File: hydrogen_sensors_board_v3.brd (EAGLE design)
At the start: 100 x 100 mm, 97 parts, among them CN1 1X4-CLEANBIG, IC1 317T, IC2 LM741D, U1 ATMEGA328P_TQFP, Y1 16MHz

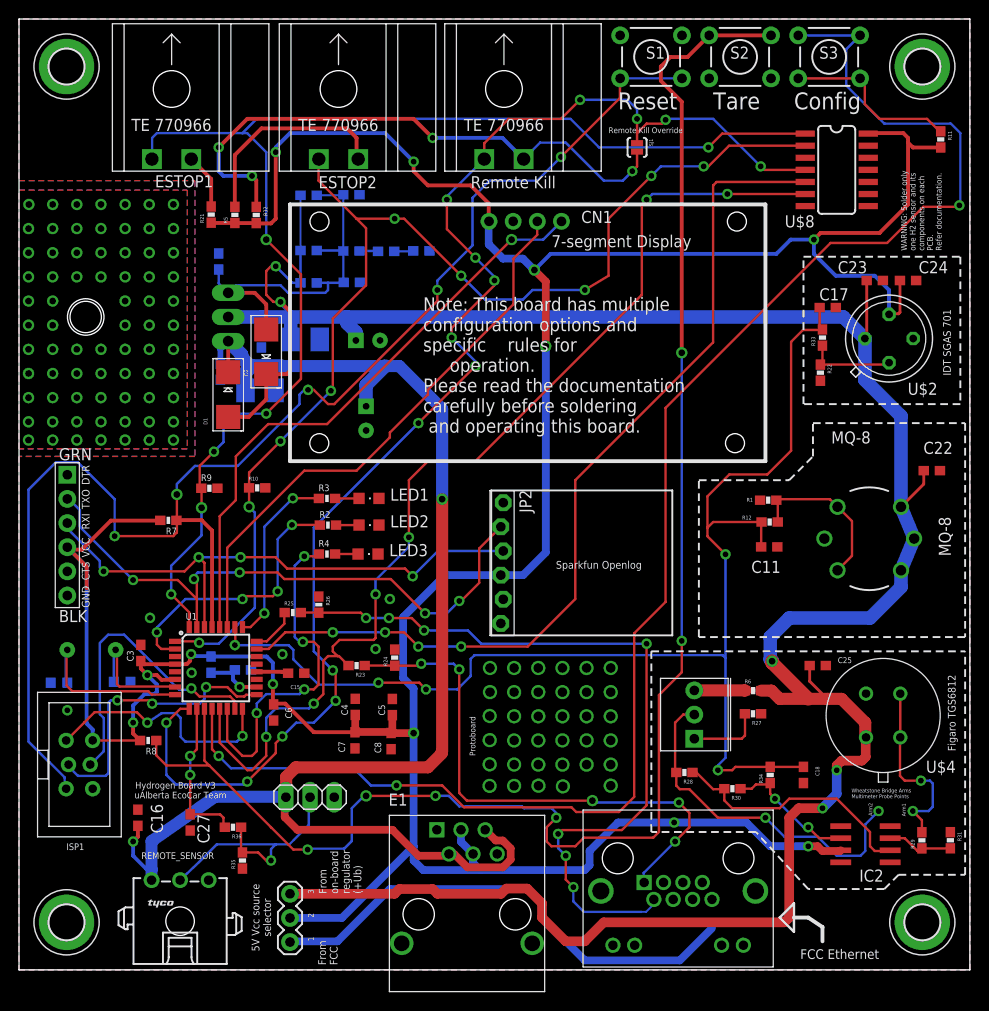
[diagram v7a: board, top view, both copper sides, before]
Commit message: routed ESTOP Signal
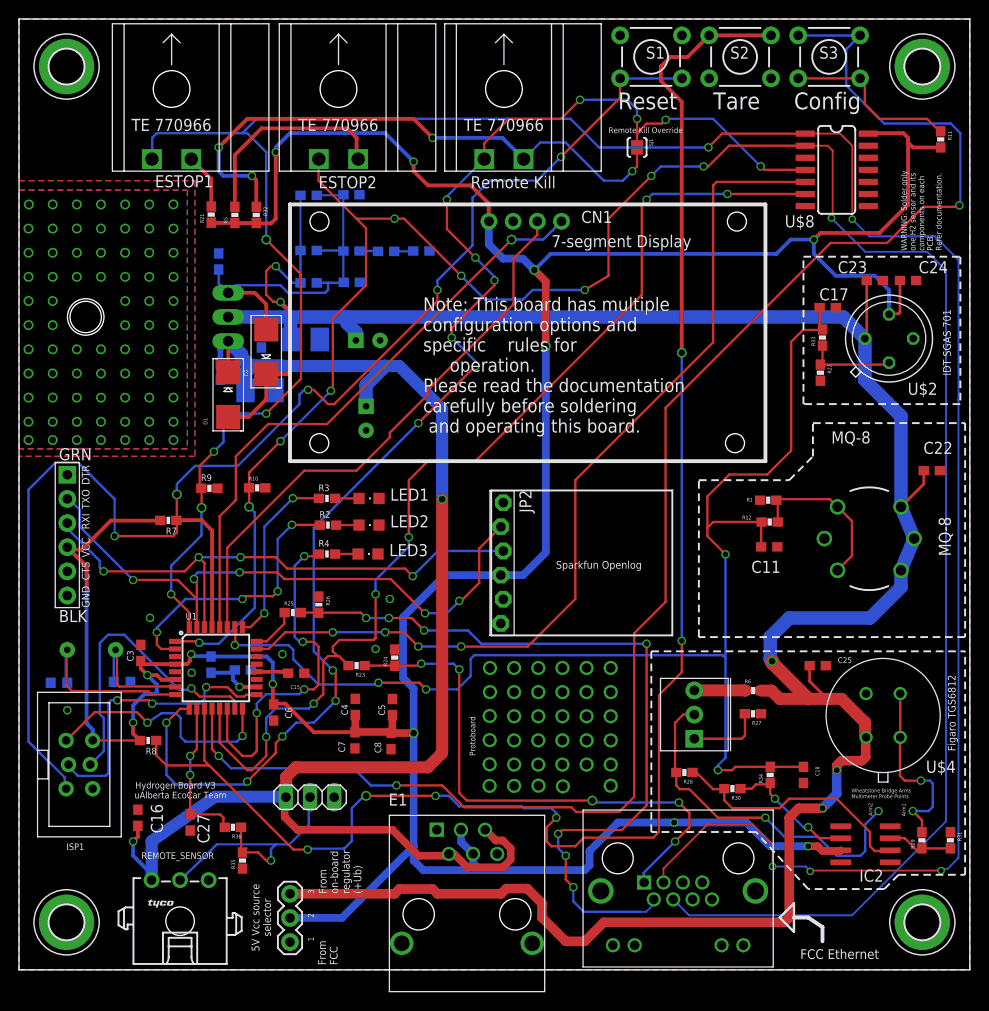
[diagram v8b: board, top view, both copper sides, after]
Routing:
- net ESTOP1: track 137.1 -> 264.9 mm, vias 6 -> 10
- net ESTOP2: track 125.4 -> 241.4 mm, vias 9 -> 10
- net 5V_FROM_FCC: track 52.9 -> 0.43 mm
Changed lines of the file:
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@@
 </class>
 </classes>
-<designrules name="SparkFun">
+<designrules name="SeeedStudio_2layer_DRU_no_angle_20140221">
+<description language="de">&lt;b&gt;EAGLE Design Rules&lt;/b&gt;
+&lt;p&gt;
+Die Standard-Design-Rules sind so gewählt, dass sie für
+die meisten Anwendungen passen. Sollte ihre Platine
+besondere Anforderungen haben, treffen Sie die erforderlichen
+Einstellungen hier und speichern die Design Rules unter
+einem neuen Namen ab.</description>
 <description language="en">&lt;b&gt;EAGLE Design Rules&lt;/b&gt;
 &lt;p&gt;
@@
 necessary adjustments and save your customized
 design rules under a new name.</description>
+<description language="zh">&lt;b&gt;Seeed Studio EAGLE Design Rules&lt;/b&gt;
+</description>
 <param name="layerSetup" value="(1*16)"/>
-<param name="mtCopper" value="0.035mm 0.035mm 0.035mm 0.035mm 0.035mm 0.035mm 0.035mm 0.035mm 0.035mm 0.035mm 0.035mm 0.035mm 0.035mm 0.035mm 0.035mm 0.035mm"/>
-<param name="mtIsolate" value="1.5mm 0.15mm 0.2mm 0.15mm 0.2mm 0.15mm 0.2mm 0.15mm 0.2mm 0.15mm 0.2mm 0.15mm 0.2mm 0.15mm 0.2mm"/>
-<param name="mdWireWire" value="8mil"/>
-<param name="mdWirePad" value="8mil"/>
-<param name="mdWireVia" value="8mil"/>
-<param name="mdPadPad" value="8mil"/>
-<param name="mdPadVia" value="8mil"/>
-<param name="mdViaVia" value="8mil"/>
-<param name="mdSmdPad" value="8mil"/>
-<param name="mdSmdVia" value="8mil"/>
-<param name="mdSmdSmd" value="8mil"/>
+<param name="mtCopper" value="0.035mm 0.0175mm 0.035mm 0.035mm 0.035mm 0.035mm 0.035mm 0.035mm 0.035mm 0.035mm 0.035mm 0.035mm 0.035mm 0.035mm 0.0175mm 0.035mm"/>
+<param name="mtIsolate" value="1.5mm 1.1mm 0.2mm 0.15mm 0.2mm 0.15mm 0.2mm 0.15mm 0.2mm 0.15mm 0.2mm 0.15mm 0.2mm 0.15mm 0.2mm"/>
+<param name="mdWireWire" value="6mil"/>
+<param name="mdWirePad" value="6mil"/>
+<param name="mdWireVia" value="6mil"/>
+<param name="mdPadPad" value="6mil"/>
+<param name="mdPadVia" value="6mil"/>
+<param name="mdViaVia" value="6mil"/>
+<param name="mdSmdPad" value="0mil"/>
+<param name="mdSmdVia" value="0mil"/>
+<param name="mdSmdSmd" value="0mil"/>
 <param name="mdViaViaSameLayer" value="8mil"/>
 <param name="mnLayersViaInSmd" value="2"/>
 <param name="mdCopperDimension" value="10mil"/>
-<param name="mdDrill" value="8mil"/>
+<param name="mdDrill" value="10mil"/>
 <param name="mdSmdStop" value="0mil"/>
-<param name="msWidth" value="8mil"/>
-<param name="msDrill" value="20mil"/>
-<param name="msMicroVia" value="9.99mm"/>
+<param name="msWidth" value="6mil"/>
+<param name="msDrill" value="12mil"/>
+<param name="msMicroVia" value="12mil"/>
 <param name="msBlindViaRatio" value="0.5"/>
 <param name="rvPadTop" value="0.25"/>
@@
 <param name="rvMicroViaOuter" value="0.25"/>
 <param name="rvMicroViaInner" value="0.25"/>
-<param name="rlMinPadTop" value="12mil"/>
+<param name="rlMinPadTop" value="10mil"/>
 <param name="rlMaxPadTop" value="20mil"/>
 <param name="rlMinPadInner" value="10mil"/>
 <param name="rlMaxPadInner" value="20mil"/>
-<param name="rlMinPadBottom" value="12mil"/>
+<param name="rlMinPadBottom" value="10mil"/>
 <param name="rlMaxPadBottom" value="20mil"/>
-<param name="rlMinViaOuter" value="10mil"/>
+<param name="rlMinViaOuter" value="6mil"/>
 <param name="rlMaxViaOuter" value="20mil"/>
-<param name="rlMinViaInner" value="10mil"/>
+<param name="rlMinViaInner" value="6mil"/>
 <param name="rlMaxViaInner" value="20mil"/>
 <param name="rlMinMicroViaOuter" value="4mil"/>
@@
 <param name="psTop" value="-1"/>
 <param name="psBottom" value="-1"/>
-<param name="psFirst" value="-1"/>
+<param name="psFirst" value="0"/>
 <param name="psElongationLong" value="100"/>
 <param name="psElongationOffset" value="100"/>
 <param name="mvStopFrame" value="1"/>
 <param name="mvCreamFrame" value="0"/>
-<param name="mlMinStopFrame" value="4mil"/>
-<param name="mlMaxStopFrame" value="4mil"/>
+<param name="mlMinStopFrame" value="2mil"/>
+<param name="mlMaxStopFrame" value="2mil"/>
 <param name="mlMinCreamFrame" value="0mil"/>
 <param name="mlMaxCreamFrame" value="0mil"/>
-<param name="mlViaStopLimit" value="25mil"/>
+<param name="mlViaStopLimit" value="100mil"/>
 <param name="srRoundness" value="0"/>
 <param name="srMinRoundness" value="0mil"/>
@@
 <param name="checkAngle" value="0"/>
 <param name="checkFont" value="1"/>
-<param name="checkRestrict" value="1"/>
+<param name="checkRestrict" value="0"/>
 <param name="checkStop" value="0"/>
 <param name="checkValues" value="0"/>
@@
 <wire x1="19" y1="50.82" x2="19.17" y2="50.65" width="0.254" layer="1"/>
 <contactref element="ETH1" pad="P$3"/>
-<wire x1="17.901" y1="36.0426" x2="67.78" y2="9.19" width="0" layer="19" extent="1-1"/>
+<wire x1="82.6853" y1="87.945" x2="86.3498" y2="87.945" width="0.2032" layer="1"/>
+<wire x1="86.3498" y1="87.945" x2="87.63" y2="86.6648" width="0.2032" layer="1"/>
+<wire x1="87.63" y1="86.6648" x2="87.63" y2="79.0194" width="0.2032" layer="1"/>
+<wire x1="87.63" y1="79.0194" x2="87.63" y2="78.9432" width="0.2032" layer="1"/>
+<via x="87.63" y="78.9432" extent="1-16" drill="0.508"/>
+<wire x1="87.63" y1="78.9432" x2="89.4334" y2="77.1398" width="0.2032" layer="16"/>
+<wire x1="89.4334" y1="77.1398" x2="95.4024" y2="77.1398" width="0.2032" layer="16"/>
+<wire x1="95.4024" y1="77.1398" x2="95.6056" y2="77.1398" width="0.2032" layer="16"/>
+<wire x1="95.4024" y1="77.1398" x2="96.3422" y2="77.1398" width="0.2032" layer="16"/>
+<wire x1="96.3422" y1="77.1398" x2="98.806" y2="74.676" width="0.2032" layer="16"/>
+<wire x1="98.806" y1="74.676" x2="98.806" y2="59.9694" width="0.2032" layer="16"/>
+<wire x1="98.806" y1="59.9694" x2="98.7298" y2="59.8932" width="0.2032" layer="16"/>
+<wire x1="98.806" y1="59.9694" x2="98.806" y2="11.7856" width="0.2032" layer="16"/>
+<wire x1="98.806" y1="11.7856" x2="97.6376" y2="10.6172" width="0.2032" layer="16"/>
+<wire x1="97.6376" y1="10.6172" x2="97.155" y2="10.6172" width="0.2032" layer="16"/>
+<wire x1="97.155" y1="10.6172" x2="96.9772" y2="10.4394" width="0.2032" layer="16"/>
+<via x="96.9772" y="10.4394" extent="1-16" drill="0.508"/>
+<wire x1="96.9772" y1="10.4394" x2="83.2866" y2="10.4394" width="0.2032" layer="1"/>
+<wire x1="83.2866" y1="10.4394" x2="83.2104" y2="10.3632" width="0.2032" layer="1"/>
+<via x="83.2104" y="10.3632" extent="1-16" drill="0.508"/>
+<wire x1="83.2104" y1="10.3632" x2="82.7024" y2="10.8712" width="0.2032" layer="16"/>
+<wire x1="82.7024" y1="10.8712" x2="79.248" y2="10.8712" width="0.2032" layer="16"/>
+<via x="79.248" y="10.8712" extent="1-16" drill="0.508"/>
+<wire x1="79.248" y1="10.8712" x2="79.248" y2="13.1826" width="0.2032" layer="1"/>
+<wire x1="79.248" y1="13.1826" x2="77.1144" y2="15.3162" width="0.2032" layer="1"/>
+<wire x1="77.1144" y1="15.3162" x2="72.5932" y2="15.3162" width="0.2032" layer="1"/>
+<wire x1="72.5932" y1="15.3162" x2="72.517" y2="15.3924" width="0.2032" layer="1"/>
+<wire x1="72.517" y1="15.3924" x2="67.78" y2="10.6554" width="0.2032" layer="1"/>
+<wire x1="67.78" y1="10.6554" x2="67.78" y2="9.19" width="0.2032" layer="1"/>
 </signal>
 <signal name="ESTOP2">
@@
 <wire x1="19.05" y1="34.3" x2="18.95" y2="34.4" width="0.254" layer="16"/>
 <contactref element="ETH1" pad="P$4"/>
-<wire x1="24.8" y1="38.1" x2="68.8" y2="7.41" width="0" layer="19" extent="16-16"/>
+<wire x1="82.6853" y1="86.675" x2="85.0544" y2="86.675" width="0.2032" layer="1"/>
+<wire x1="85.0544" y1="86.675" x2="85.5726" y2="86.1568" width="0.2032" layer="1"/>
+<wire x1="85.5726" y1="86.1568" x2="85.5726" y2="79.1972" width="0.2032" layer="1"/>
+<wire x1="85.5726" y1="79.1972" x2="85.4456" y2="79.0702" width="0.2032" layer="1"/>
+<via x="85.4456" y="79.0702" extent="1-16" drill="0.508"/>
+<wire x1="85.4456" y1="79.0702" x2="89.0016" y2="75.5142" width="0.2032" layer="16"/>
+<wire x1="89.0016" y1="75.5142" x2="95.5294" y2="75.5142" width="0.2032" layer="16"/>
+<wire x1="95.5294" y1="75.5142" x2="97.4852" y2="73.5584" width="0.2032" layer="16"/>
+<wire x1="97.4852" y1="15.621" x2="87.6046" y2="5.7404" width="0.2032" layer="16"/>
+<wire x1="87.6046" y1="5.7404" x2="70.4696" y2="5.7404" width="0.2032" layer="16"/>
+<wire x1="70.4696" y1="5.7404" x2="68.8" y2="7.41" width="0.2032" layer="16"/>
+<wire x1="97.4852" y1="73.5584" x2="97.4852" y2="15.621" width="0.2032" layer="16"/>
 </signal>
 <signal name="H2_REMOTE">
@@
 <signal name="5V_FROM_FCC">
 <contactref element="JP5" pad="3"/>
-<wire x1="72.88" y1="4.38" x2="69.5" y2="1" width="0.8128" layer="16"/>
-<wire x1="69.5" y1="1" x2="59.5" y2="1" width="0.8128" layer="16"/>
-<wire x1="59.5" y1="1" x2="55" y2="5.5" width="0.8128" layer="16"/>
-<wire x1="55" y1="5.5" x2="55" y2="7" width="0.8128" layer="16"/>
-<wire x1="55" y1="7" x2="53.5" y2="8.5" width="0.8128" layer="16"/>
-<wire x1="53.5" y1="8.5" x2="39" y2="8.5" width="0.8128" layer="16"/>
-<wire x1="39" y1="8.5" x2="33.5" y2="3" width="0.8128" layer="16"/>
-<wire x1="33.5" y1="3" x2="28.08" y2="3" width="0.8128" layer="16"/>
 <wire x1="28.08" y1="3" x2="28.5" y2="2.92" width="0.8128" layer="16"/>
 </signal>
